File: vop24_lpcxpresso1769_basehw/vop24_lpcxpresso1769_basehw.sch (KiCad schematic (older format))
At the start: 6 parts, among them J1 Micro_SD_Card, J2 Conn_01x05_Male, J3 Conn_01x06_Male, U1 LPCXpresso1769

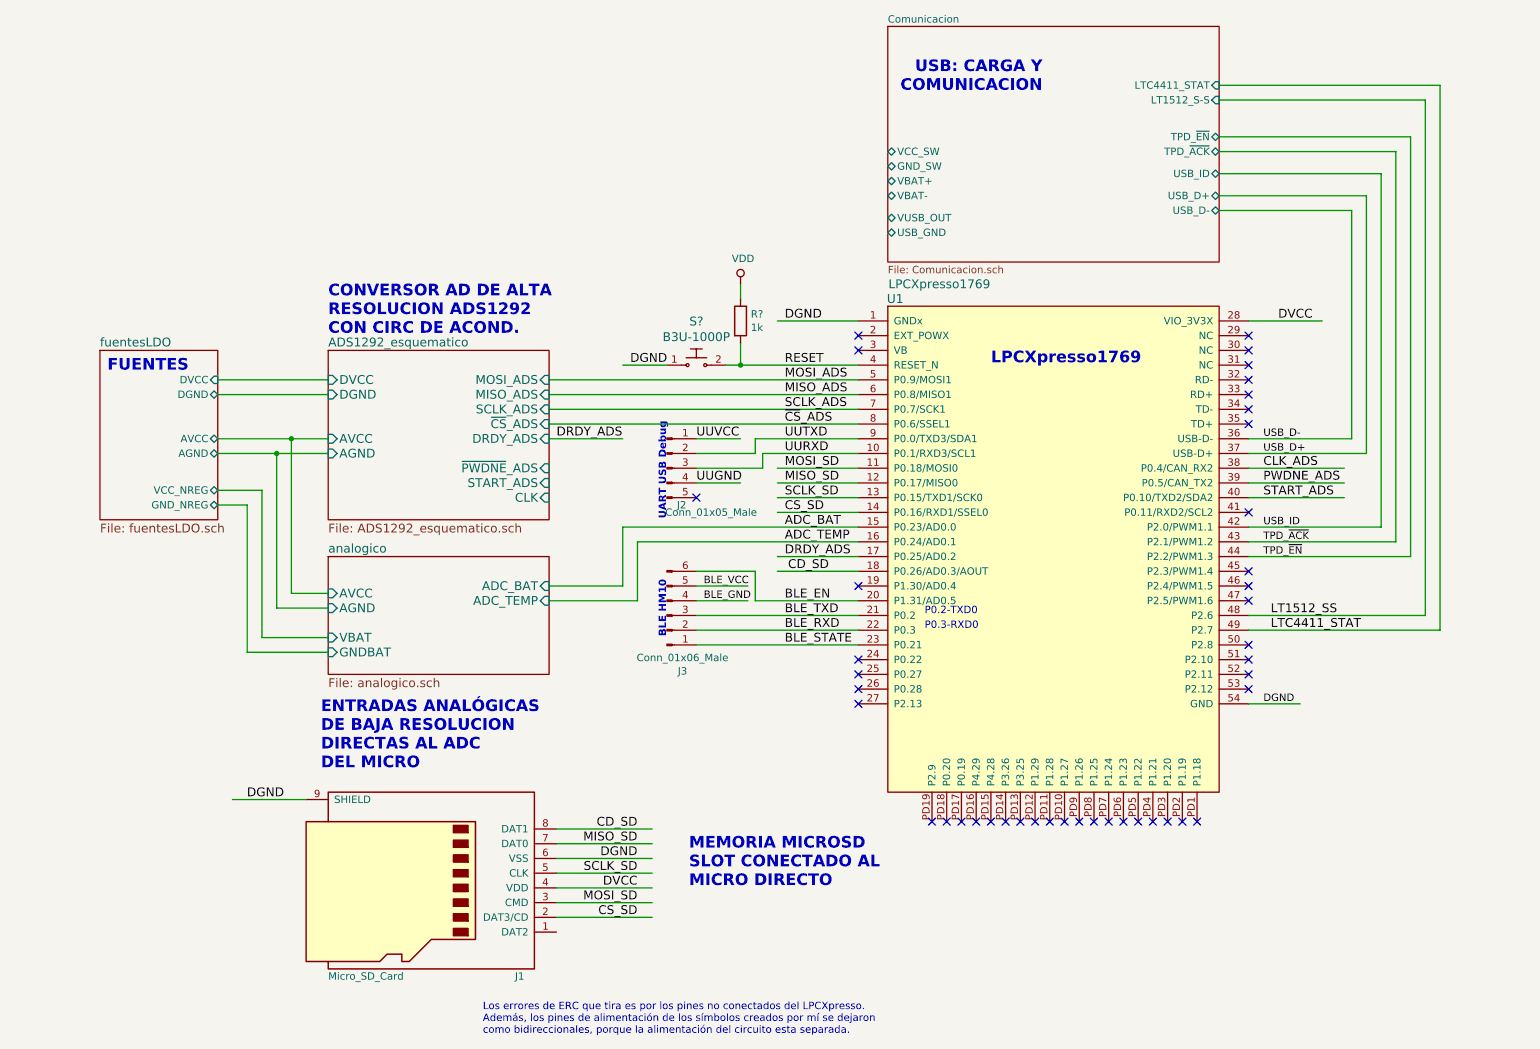
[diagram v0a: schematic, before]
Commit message: ESQ: modificaciones de etiquetas. Falta cambiar todas las conexiones de vcc
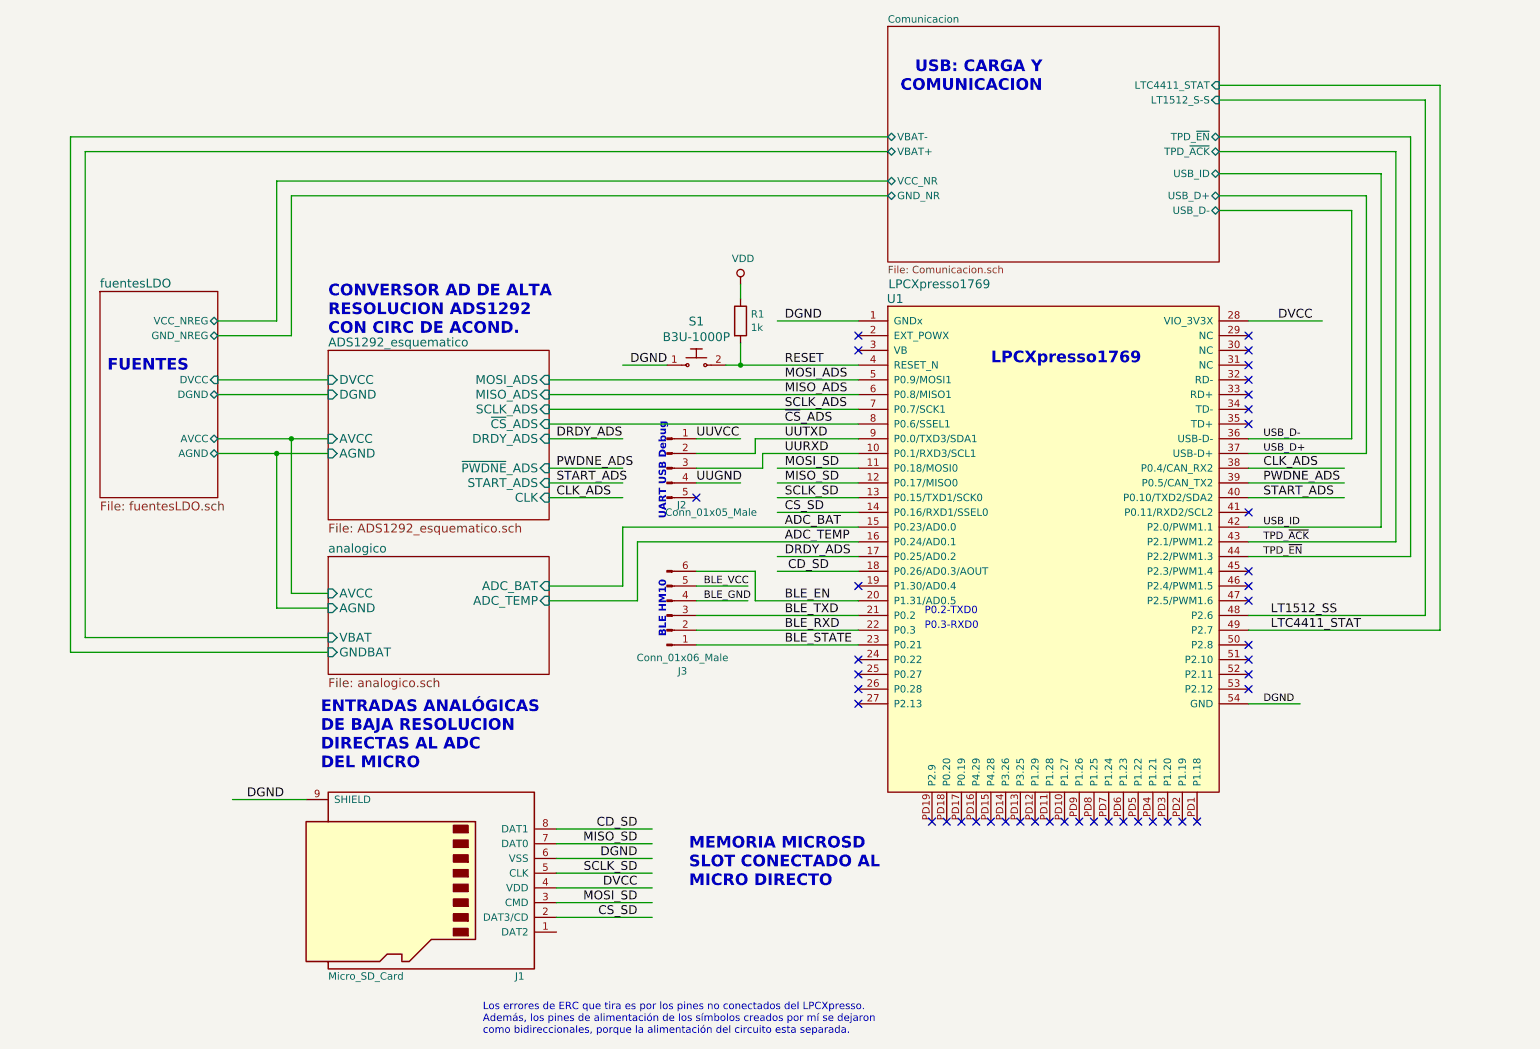
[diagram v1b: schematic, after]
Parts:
- gave numbers to parts that had none: 2
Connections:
- wire segments 89 -> 98
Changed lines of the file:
@@
 USB_ID
 $Sheet
-S 1000 2950 800  1150
+S 1000 2550 800  1400
 U 5B3826CA
 F0 "fuentesLDO" 60
@@
 F4 "DGND" B R 1800 3250 50
 F5 "DVCC" I R 1800 3150 50
-F6 "VCC_NREG" B R 1800 3900 50
-F7 "GND_NREG" B R 1800 4000 50
+F6 "VCC_NREG" B R 1800 2750 50
+F7 "GND_NREG" B R 1800 2850 50
 $EndSheet
 $Sheet
@@
 F0 "Comunicacion" 50
 F1 "Comunicacion.sch" 50
-F2 "VUSB_OUT" B L 6350 2050 50
-F3 "TPD_~EN" B R 8600 1500 50
-F4 "TPD_~ACK" B R 8600 1600 50
-F5 "USB_D+" B R 8600 1900 50
-F6 "USB_D-" B R 8600 2000 50
-F7 "USB_ID" B R 8600 1750 50
-F8 "USB_GND" B L 6350 2150 50
-F9 "VBAT-" B L 6350 1900 50
-F10 "VBAT+" B L 6350 1800 50
-F11 "VCC_SW" B L 6350 1600 50
-F12 "GND_SW" B L 6350 1700 50
-F13 "LTC4411_STAT" I R 8600 1150 50
-F14 "LT1512_S-S" I R 8600 1250 50
+F2 "TPD_~EN" B R 8600 1500 50
+F3 "TPD_~ACK" B R 8600 1600 50
+F4 "USB_D+" B R 8600 1900 50
+F5 "USB_D-" B R 8600 2000 50
+F6 "USB_ID" B R 8600 1750 50
+F7 "VBAT-" B L 6350 1500 50
+F8 "VBAT+" B L 6350 1600 50
+F9 "LTC4411_STAT" I R 8600 1150 50
+F10 "LT1512_S-S" I R 8600 1250 50
+F11 "VCC_NR" B L 6350 1800 50
+F12 "GND_NR" B L 6350 1900 50
 $EndSheet
 Wire Wire Line
@@
 NoConn ~ 8800 4450
 $Comp
-L dk_Tactile-Switches:B3U-1000P S?
+L dk_Tactile-Switches:B3U-1000P S1
 U 1 1 5C0E8775
 P 5050 3050
-F 0 "S?" H 5050 3347 60  0000 C CNN
+F 0 "S1" H 5050 3347 60  0000 C CNN
 F 1 "B3U-1000P" H 5050 3241 60  0000 C CNN
 F 2 "digikey-footprints:Switch_Tactile_SMD_B3U-1000P" H 5250 3250 60  0001 L CNN
@@
 	5350 3050 6150 3050
 $Comp
-L Device:R R?
+L Device:R R1
 U 1 1 5C101D2E
 P 5350 2750
-F 0 "R?" H 5420 2796 50  0000 L CNN
+F 0 "R1" H 5420 2796 50  0000 L CNN
 F 1 "1k" H 5420 2705 50  0000 L CNN
 F 2 "" V 5280 2750 50  0001 C CNN
@@
 	5350 2600 5350 2500
 $Comp
-L power:VDD #PWR?
+L power:VDD #PWR01
 U 1 1 5BF71E9E
 P 5350 2500
-F 0 "#PWR?" H 5350 2350 50  0001 C CNN
+F 0 "#PWR01" H 5350 2350 50  0001 C CNN
 F 1 "VDD" H 5367 2673 50  0000 C CNN
 F 2 "" H 5350 2500 50  0001 C CNN
@@
 	1800 3250 2550 3250
 Wire Wire Line
-	1800 4000 2000 4000
-Wire Wire Line
-	2000 5000 2550 5000
-Wire Wire Line
-	2000 4000 2000 5000
-Wire Wire Line
-	2550 4900 2100 4900
-Wire Wire Line
-	2100 4900 2100 3900
-Wire Wire Line
-	2100 3900 1800 3900
-Wire Wire Line
 	2550 4700 2200 4700
 Wire Wire Line
@@
 Wire Wire Line
 	8800 4850 10100 4850
+Wire Wire Line
+	4050 3750 4550 3750
+Wire Wire Line
+	4050 3850 4550 3850
+Wire Wire Line
+	4050 3950 4550 3950
+Text Label 4100 3750 0    60   ~ 0
+PWDNE_ADS
+Text Label 4100 3850 0    60   ~ 0
+START_ADS
+Text Label 4100 3950 0    60   ~ 0
+CLK_ADS
+Wire Wire Line
+	6350 1800 2200 1800
+Wire Wire Line
+	2200 1800 2200 2750
+Wire Wire Line
+	2200 2750 1800 2750
+Wire Wire Line
+	1800 2850 2300 2850
+Wire Wire Line
+	2300 1900 6350 1900
+Wire Wire Line
+	2300 1900 2300 2850
+Wire Wire Line
+	2550 4900 900  4900
+Wire Wire Line
+	900  4900 900  1600
+Wire Wire Line
+	900  1600 6350 1600
+Wire Wire Line
+	6350 1500 800  1500
+Wire Wire Line
+	800  1500 800  5000
+Wire Wire Line
+	800  5000 2550 5000
 $EndSCHEMATC

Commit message: ESQ: cambios sobre etiquetas y simbolos de POWER
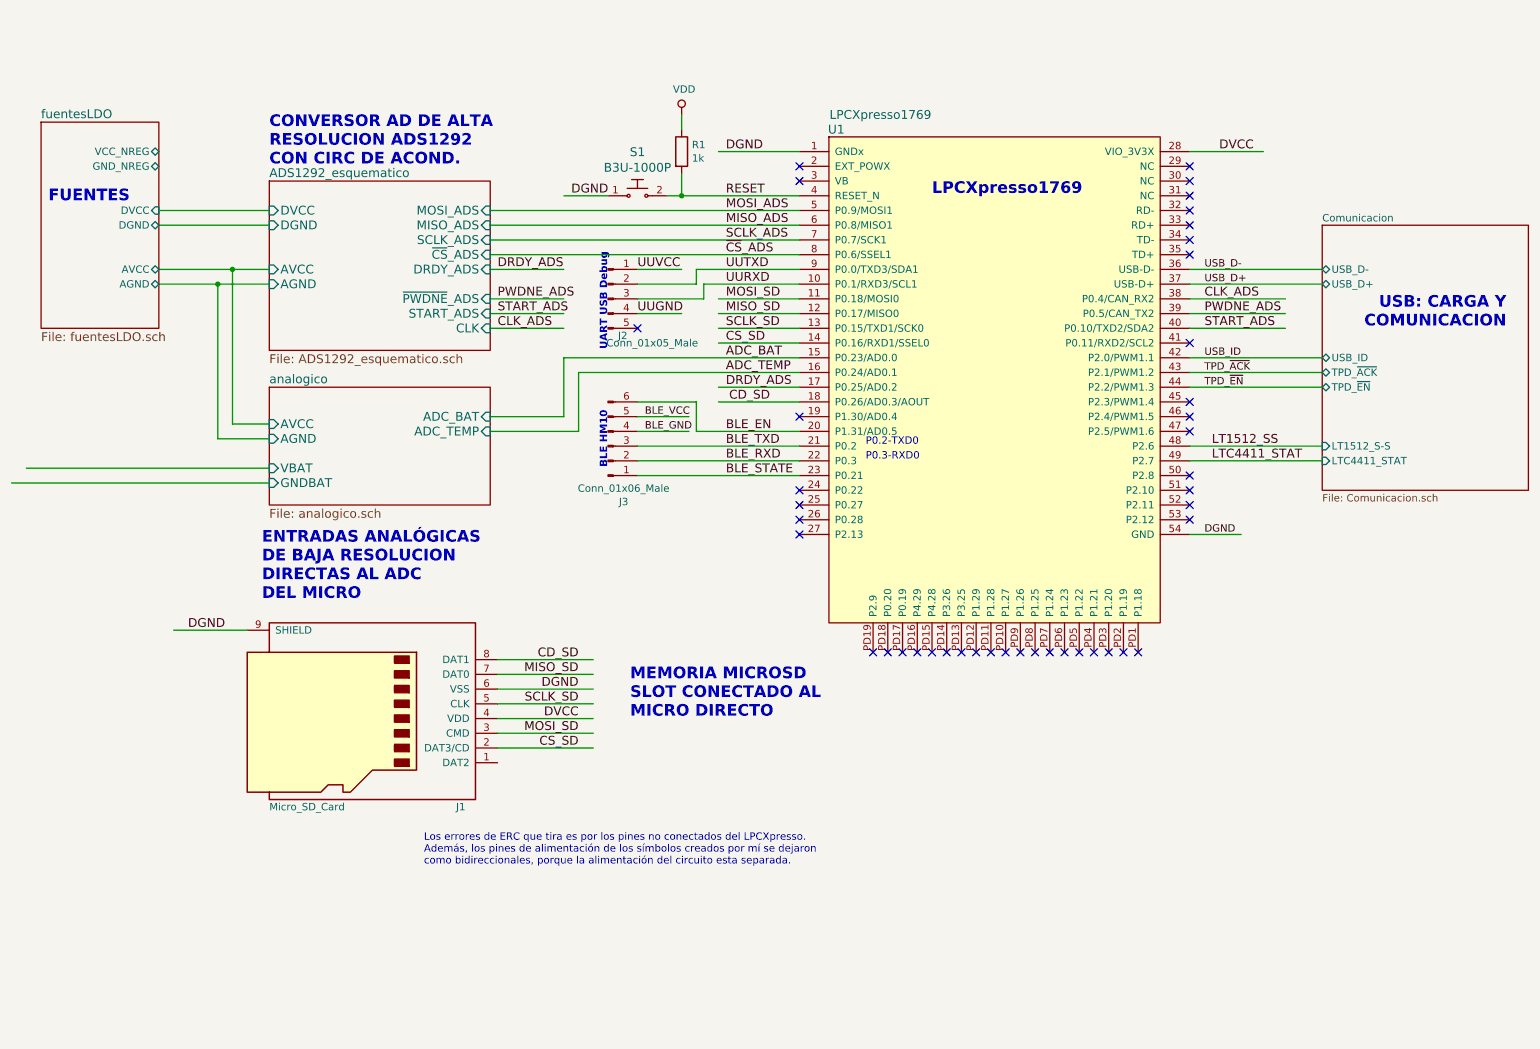
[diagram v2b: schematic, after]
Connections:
- wire segments 98 -> 74
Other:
- moved on the sheet: J1, J2, J3, R1, S1, U1

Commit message: ESQ: todas las correcciones atendidas
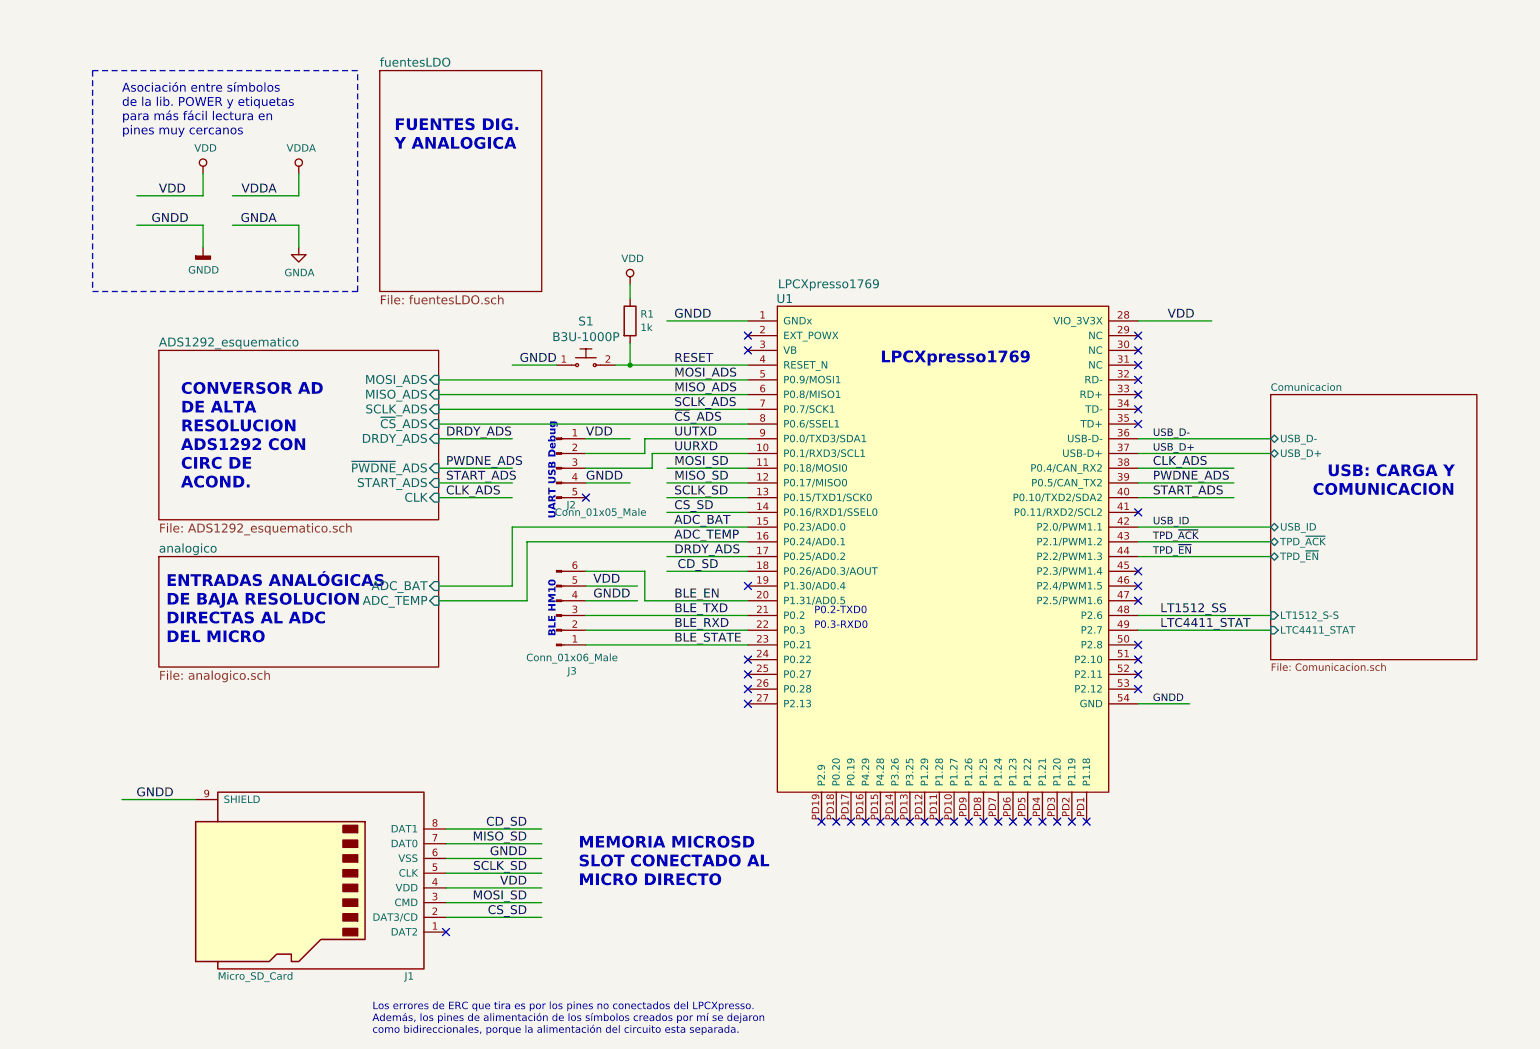
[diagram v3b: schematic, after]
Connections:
- net labels added: GNDA, GNDD, VDDA
- net labels removed: BLE_GND, BLE_VCC, DGND, DVCC, UUGND, UUVCC
- wire segments 74 -> 70
- no-connect marks 42 -> 43
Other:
- note added: "Asociación entre símbolos\nde la lib. POWER y etiquetas\npara más fácil lectura en \npines muy cercanos"
- note added: "CONVERSOR AD \nDE ALTA \nRESOLUCION\nADS1292 CON \nCIRC DE \nACOND."
- note added: "FUENTES DIG.\nY ANALOGICA\n"
- note removed: "CONVERSOR AD DE ALTA \nRESOLUCION ADS1292\nCON CIRC DE ACOND."
- note removed: "FUENTES"
- moved on the sheet: J1, J2, J3, R1, S1, U1

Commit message: ESQ: cambios en asociaciones de footprints
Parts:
- R1: footprint (none) -> Resistor_SMD:R_0805_2012Metric_Pad1.15x1.40mm_HandSolder
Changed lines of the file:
@@
 F 0 "R1" H 4670 2796 50  0000 L CNN
 F 1 "1k" H 4670 2705 50  0000 L CNN
-F 2 "" V 4530 2750 50  0001 C CNN
+F 2 "Resistor_SMD:R_0805_2012Metric_Pad1.15x1.40mm_HandSolder" V 4530 2750 50  0001 C CNN
 F 3 "~" H 4600 2750 50  0001 C CNN
 	1    4600 2750

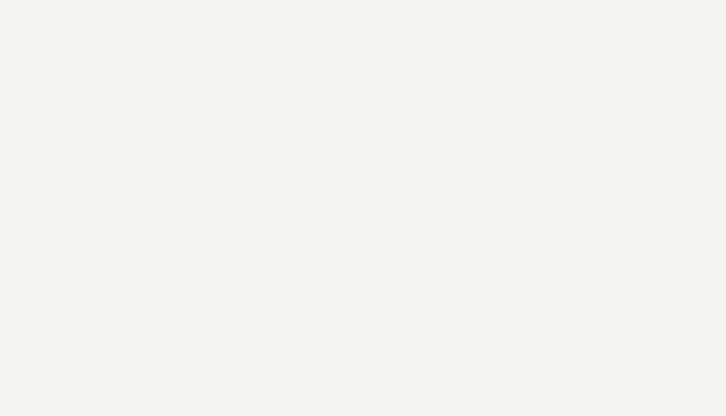
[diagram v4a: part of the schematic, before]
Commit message: ESQ: cambios en net-tie y footprints PCB: cambios grandes de dimensiones y ruteo
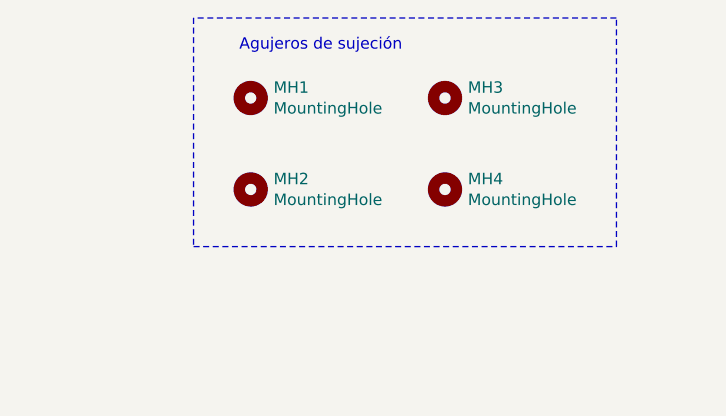
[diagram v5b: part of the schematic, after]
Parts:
- added MH1, MH2, MH3, MH4: MountingHole, MountingHole:MountingHole_3.5mm, symbol Mechanical:MountingHole
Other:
- note added: "Agujeros de sujeción"
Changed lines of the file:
@@
 GNDD
 NoConn ~ 3350 6900
+$Comp
+L Mechanical:MountingHole MH3
+U 1 1 5BFE9A50
+P 9200 1050
+F 0 "MH3" H 9300 1096 50  0000 L CNN
+F 1 "MountingHole" H 9300 1005 50  0000 L CNN
+F 2 "MountingHole:MountingHole_3.5mm" H 9200 1050 50  0001 C CNN
+F 3 "~" H 9200 1050 50  0001 C CNN
+	1    9200 1050
+	1    0    0    -1
+$EndComp
+$Comp
+L Mechanical:MountingHole MH4
+U 1 1 5BFE9AC3
+P 9200 1450
+F 0 "MH4" H 9300 1496 50  0000 L CNN
+F 1 "MountingHole" H 9300 1405 50  0000 L CNN
+F 2 "MountingHole:MountingHole_3.5mm" H 9200 1450 50  0001 C CNN
+F 3 "~" H 9200 1450 50  0001 C CNN
+	1    9200 1450
+	1    0    0    -1
+$EndComp
+$Comp
+L Mechanical:MountingHole MH1
+U 1 1 5BFE9AFF
+P 8350 1050
+F 0 "MH1" H 8450 1096 50  0000 L CNN
+F 1 "MountingHole" H 8450 1005 50  0000 L CNN
+F 2 "MountingHole:MountingHole_3.5mm" H 8350 1050 50  0001 C CNN
+F 3 "~" H 8350 1050 50  0001 C CNN
+	1    8350 1050
+	1    0    0    -1
+$EndComp
+$Comp
+L Mechanical:MountingHole MH2
+U 1 1 5BFE9B3F
+P 8350 1450
+F 0 "MH2" H 8450 1496 50  0000 L CNN
+F 1 "MountingHole" H 8450 1405 50  0000 L CNN
+F 2 "MountingHole:MountingHole_3.5mm" H 8350 1450 50  0001 C CNN
+F 3 "~" H 8350 1450 50  0001 C CNN
+	1    8350 1450
+	1    0    0    -1
+$EndComp
+Wire Notes Line
+	8100 1700 9950 1700
+Wire Notes Line
+	9950 1700 9950 700
+Wire Notes Line
+	9950 700  8100 700
+Wire Notes Line
+	8100 700  8100 1700
+Text Notes 8300 850  0    50   ~ 0
+Agujeros de sujeción
 $EndSCHEMATC
